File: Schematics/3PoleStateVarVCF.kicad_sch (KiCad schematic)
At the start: 127 parts, among them J54 Conn_01x04, J55 Conn_01x03, U270 DG212C, U277 DG212C, U32 SSI2164, U33 TL072, U34 TL074, U35 TL074, U36 TL074, U37 TL072, U38 TL074, U39 SSI2164, U42 TL072, U43 TL072

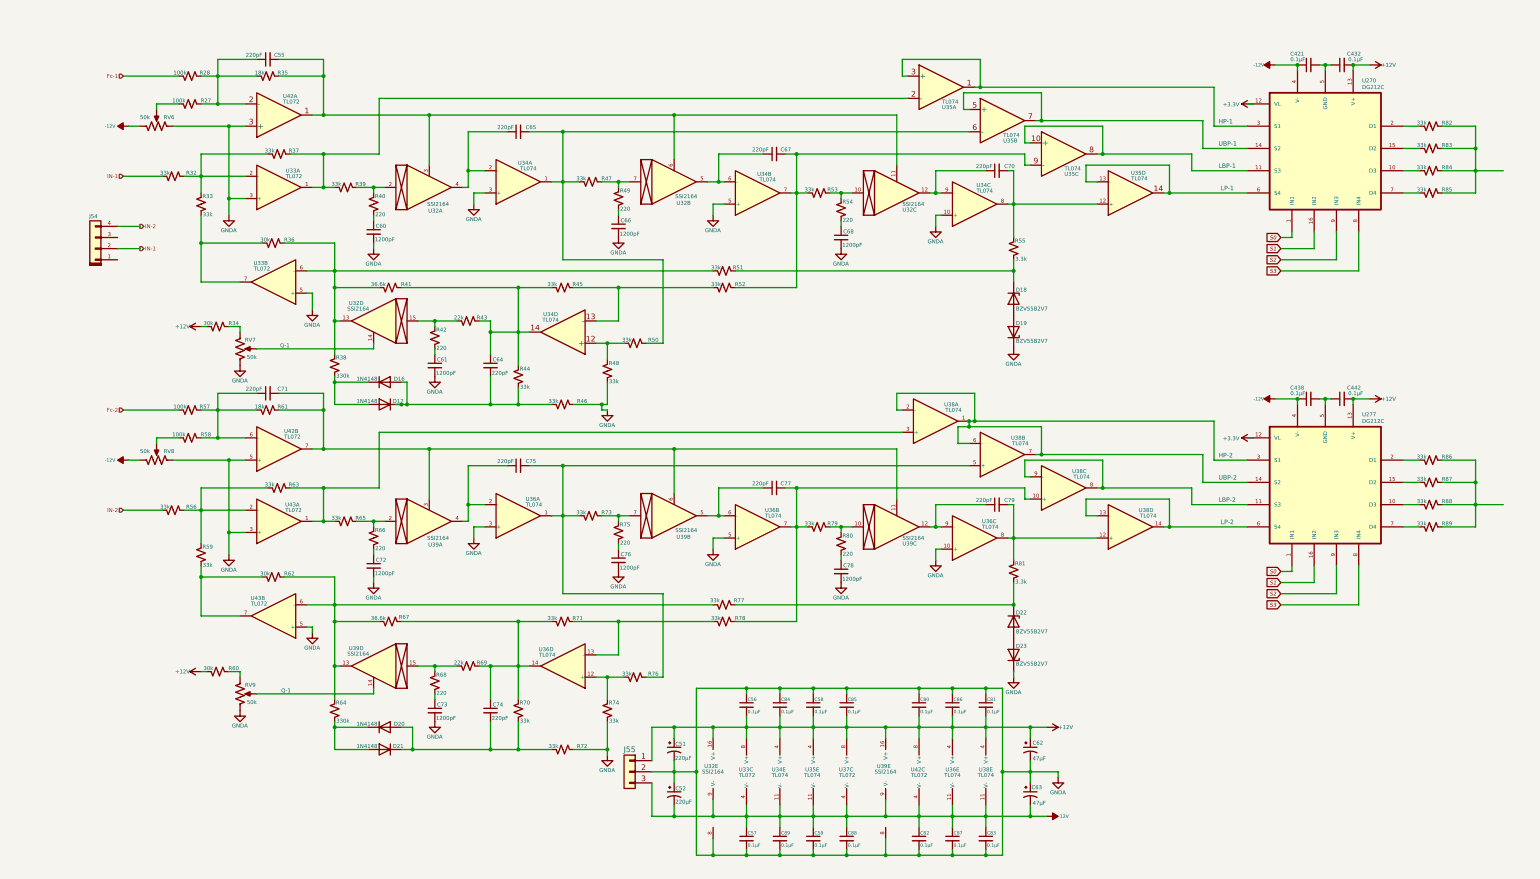
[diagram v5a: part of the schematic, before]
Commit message: Finalized first filter design.  Setep for filter testing.
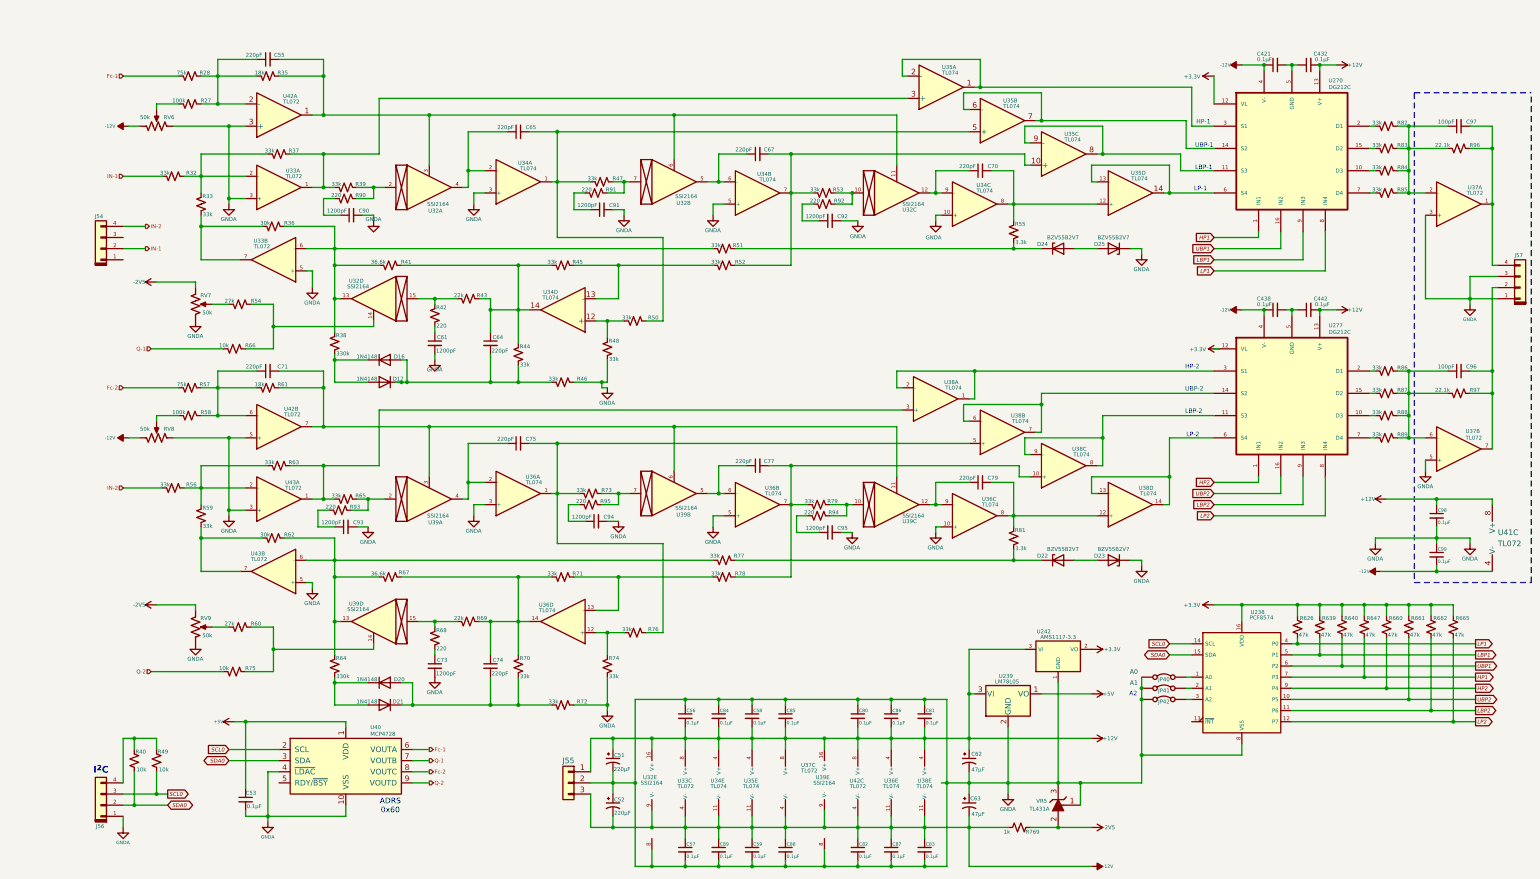
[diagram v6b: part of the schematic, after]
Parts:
- removed C60, C66, C68, C72, C76, C78: 1200pF, symbol Device:C_Small
- removed D18, D19: BZV55B2V7, Diode_SMD:D_MiniMELF, symbol Diode:BZV55B2V7
- removed R34: 30k, symbol Device:R_Small_US
- removed R80: 220, symbol Device:R_Small_US
- added C53, C98, C99: 0.1µF, symbol Device:C_Small
- added C90, C91, C92, C93, C94, C95: 1200pF, symbol Device:C_Small
- added C96, C97: 100pF, symbol Device:C_Small
- added D24, D25: BZV55B2V7, Diode_SMD:D_MiniMELF, symbol Diode:BZV55B2V7
- added J56: Conn_01x04, symbol Connector_keyed_kicad_sym:Conn_01x04
- added J57: Conn_01x04, symbol My Connectors:Conn_01x04
- added JP40, JP41, JP42: Jumper_2_Bridged, symbol Jumper:Jumper_2_Bridged
- added R626, R639, R640, R647, R660, R661, R662, R665: 47k, symbol Device:R_Small_US
- added R769: 1k, symbol Device:R_Small_US
- added R90, R91, R92, R93, R94, R95: 220, symbol Device:R_Small_US
- added R96, R97: 22.1k, symbol Device:R_Small_US
- added U238: PCF8574, symbol Interface_Expansion:PCF8574
- added U239: LM78L05, Package_TO_SOT_THT:TO-92_Inline, symbol Regulator_Linear:LM78L05_TO92
- added U242: AMS1117-3.3, Package_TO_SOT_SMD:SOT-223-3_TabPin2, symbol Regulator_Linear:AMS1117-3.3
- added unit 2 of U37
- added unit 1 of U37
- added U40: MCP4728, Package_SO:MSOP-10_3x3mm_P0.5mm, symbol MyDac:MCP4728
- added U41: TL072, symbol Amplifier_Operational:TL072
- added VR5: TL431A, digikey-footprints:TO-92-3_Formed_Leads, symbol dk_PMIC-Voltage-Reference:TL431CLPM
- R28, R57: value 100k -> 75k
- R40, R49, R66, R75: value 220 -> 10k
- R54: value 220 -> 27k
- R60: value 30k -> 27k
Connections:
- net +12V: now also C98.1, U239.3 (VI), U242.3 (VI), U41.8 (V+); no longer R60.2
- net +3.3V: now also R626.1, R639.1, R640.1, R647.1, R660.1, R661.1, R662.1, R665.1, U238.16 (VDD), U242.2 (VO)
- net -12V: now also C99.2, R769.1, U41.4 (V-)
- net Fc-1: now also U40.6 (VOUTA)
- net Fc-2: now also U40.8 (VOUTC)
- net GNDA: now also C53.2, C90.2, C91.2, C92.2, C93.2, C94.2, C95.2, C98.2, C99.1, D25.1 (K), J56.1 (Pin_1), J57.1 (Pin_1), J57.3 (Pin_3), JP40.1 (A), JP41.1 (A), JP42.1 (A), U238.8 (VSS), U239.2 (GND), U242.1 (GND), U37.3 (+), U37.5 (+), U40.10 (VSS), U40.4 (~{LDAC}), VR5.1 (REF), VR5.3 (K)
- net at R73.1, U39.7: now also R95.1; no longer R75.1
- net Q-2: now reaches R75.2
- net Q-2: now also U40.9 (VOUTD)
- net at R82.1, R83.1, R84.1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: now also C97.1, R96.2, U37.2 (-)
- net at R53.1, U32.10: now also R92.1; no longer R54.1
- net at R54.2: now also RV7. (2)
- net at R79.1, U39.10: now also R94.1
- net at U270.14 (S2), U35.7: now also U35.6 (-); no longer U35.5 (+)
- net at C65.2, R47.2, R50.1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: now also U35.5 (+); no longer U35.6 (-)
- net at R51.1, R55.2: now also D24.1 (K)
- net at U270.11 (S3), U35.8: now also U35.9 (-); no longer U35.10 (+)
- net at U270.3 (S1), U35.1: now also U35.2 (-); no longer U35.3 (+)
- net at R86.1, R87.1, R88.1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: now also C96.1, R97.2, U37.6 (-)
- net at R39.1, U32.2: now also R90.1; no longer R40.1
- net SDA0: now reaches R40.2
- net SDA0: now also J56.2 (Pin_2), U238.15 (SDA), U40.3 (SDA)
- net at U277.14 (S2), U38.6 (-), U38.7: no longer U277.3 (S1), U38.1, U38.2 (-)
- net at C67.2, R52.1, R53.2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: now also U35.10 (+); no longer U35.9 (-)
- net at R65.1, U39.2: now also R93.1; no longer R66.1
- net Q-1: now reaches R66.2
- net Q-1: now also U40.7 (VOUTB)
- net at U32.14: now also R54.1, R66.1; no longer RV7. (2)
- net at U39.14: now also R60.1, R75.1; no longer RV9. (2)
- net at R47.1, U32.7: now also R91.1; no longer R49.1
- net SCL0: now reaches R49.2
- net SCL0: now also J56.3 (Pin_3), U238.14 (SCL), U40.2 (SCL)
- net at R37.1, R39.2, U33.1: now also U35.3 (+); no longer U35.2 (-)
- net S0 renamed HP1
- net HP1: now also R647.2, U238.7 (P3); no longer U277.1 (IN1)
- net S1 renamed UBP1
- net UBP1: now also R640.2, U238.6 (P2); no longer U277.16 (IN2)
- net S2 renamed LBP1
- net LBP1: now also R639.2, U238.5 (P1); no longer U277.9 (IN3)
- net S3 renamed LP1
- net LP1: now also R626.2, U238.4 (P0); no longer U277.8 (IN4)
- new net: C96.2, J57.2 (Pin_2), R97.1, U37.7
- new net: C97.2, J57.4 (Pin_4), R96.1, U37.1
- new net: C91.1, R91.2
- new net: C93.1, R93.2
- new net: R60.2, RV9. (2)
- new net: D24.2 (A), D25.2 (A)
- new net: JP40.2 (B), U238.1 (A0)
- new net: C92.1, R92.2
- new net: C95.1, R94.2
- new net: JP41.2 (B), U238.2 (A1)
- new net: JP42.2 (B), U238.3 (A2)
- new net: U277.3 (S1), U38.1, U38.2 (-)
- new net: C94.1, R95.2
- new net: C90.1, R90.2
- new net: J56.4 (Pin_4), R40.1, R49.1
- new net +5V: C53.1, U239.1 (VO), U40.1 (VDD)
- new net -2V5: R769.2, RV7. (2), RV9. (2), VR5.2 (A)
- new net HP2: R660.2, U238.9 (P4), U277.1 (IN1)
- new net LBP2: R662.2, U238.11 (P6), U277.9 (IN3)
- new net LP2: R665.2, U238.12 (P7), U277.8 (IN4)
- new net UBP2: R661.2, U238.10 (P5), U277.16 (IN2)
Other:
- note added: "A0"
- note added: "A1"
- note added: "A2"
- note added: "ADRS 0x60"
- note added: "I^{2}C"
- note removed: "Q-1"
- moved on the sheet: C421, C432, C438, C442, C51, C52, C56, C57, C58, C59, C61, C62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

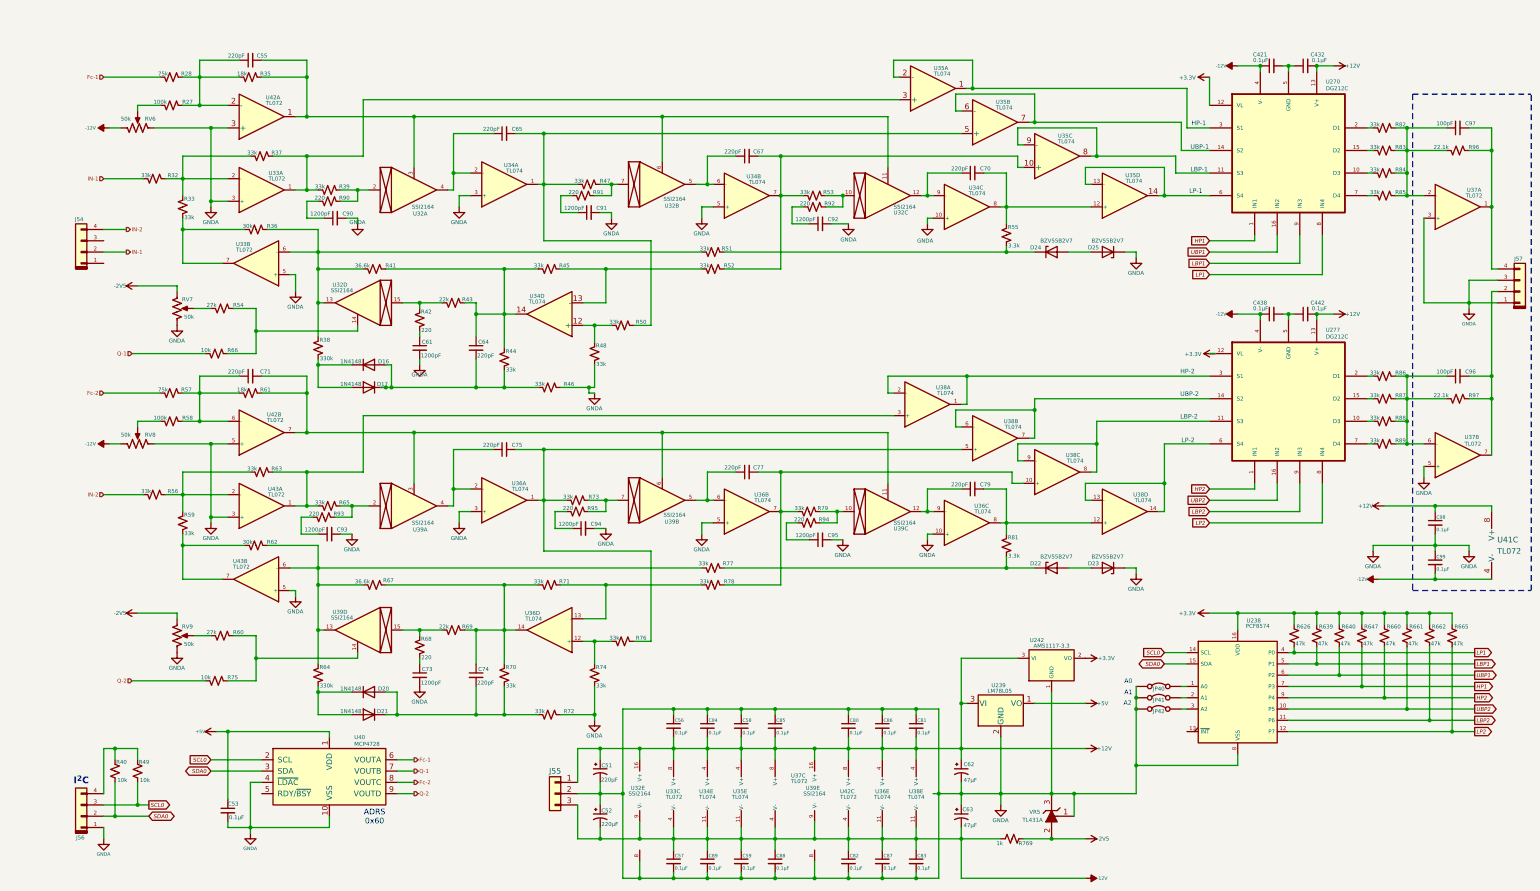
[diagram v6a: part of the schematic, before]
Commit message: Fixed schematic errors.
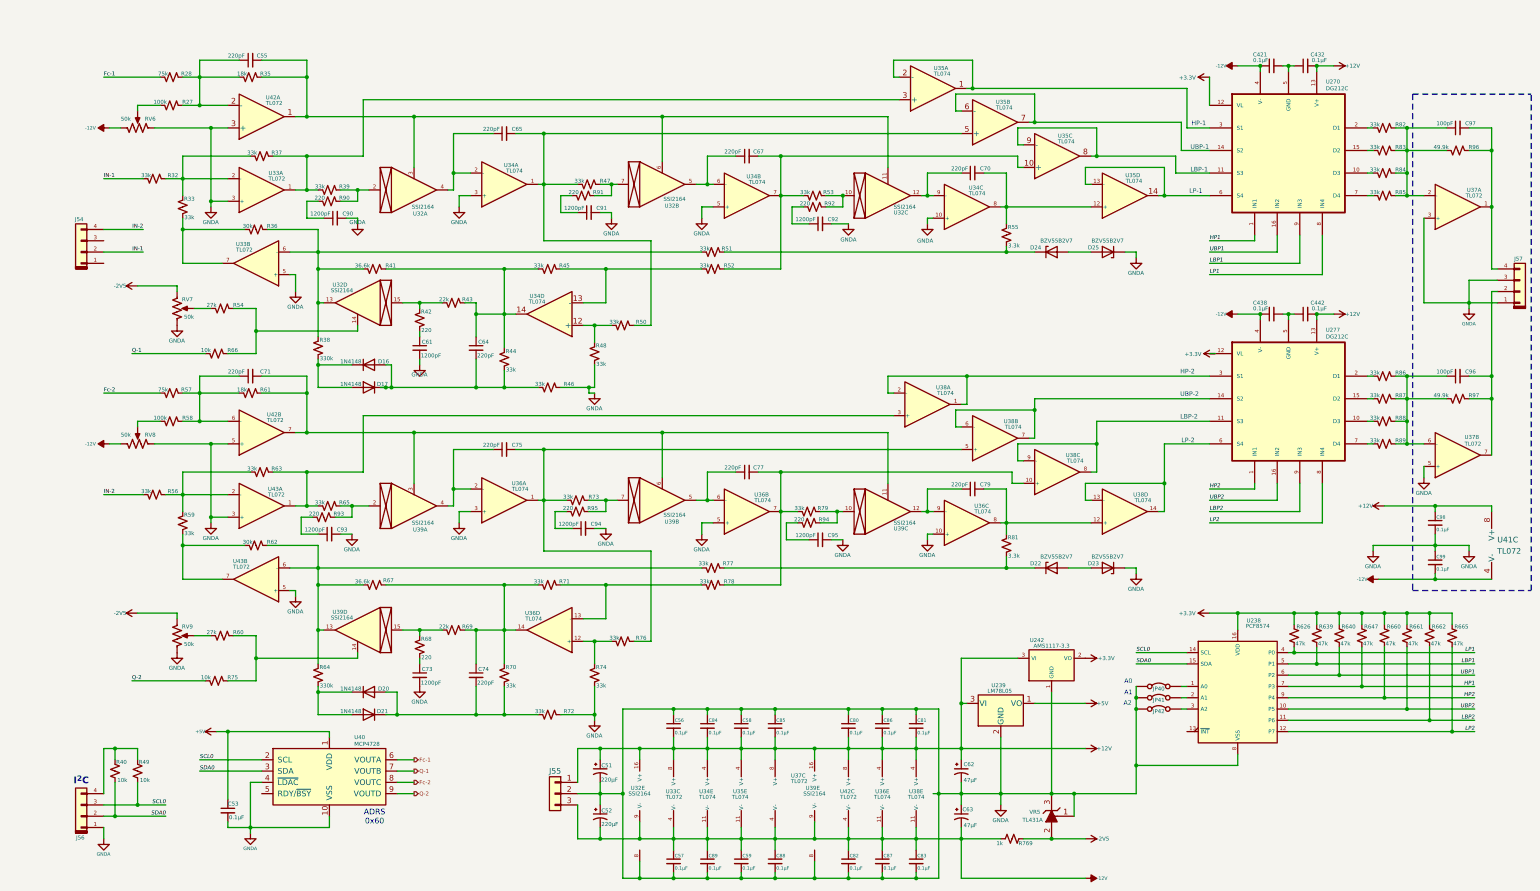
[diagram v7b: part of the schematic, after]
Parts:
- R96, R97: value 22.1k -> 49.9k

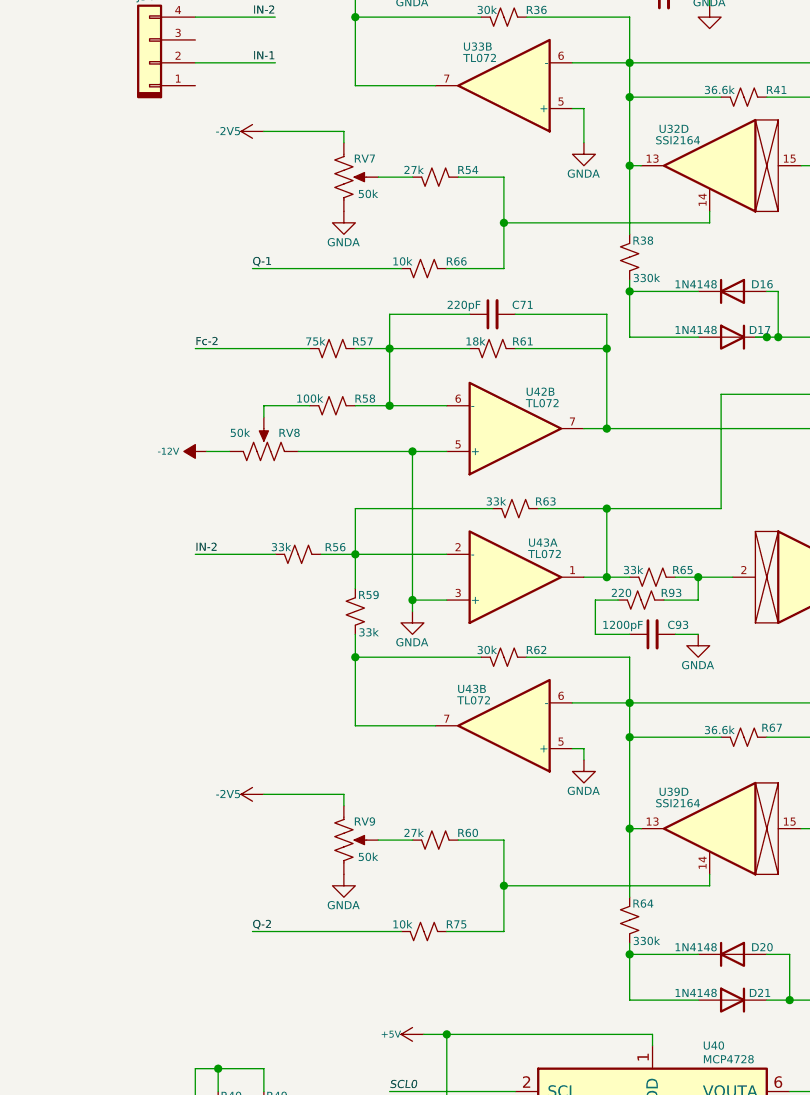
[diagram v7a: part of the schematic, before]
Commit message: Refactored hardware and software.  Improved Launch Control XL configuration and control.
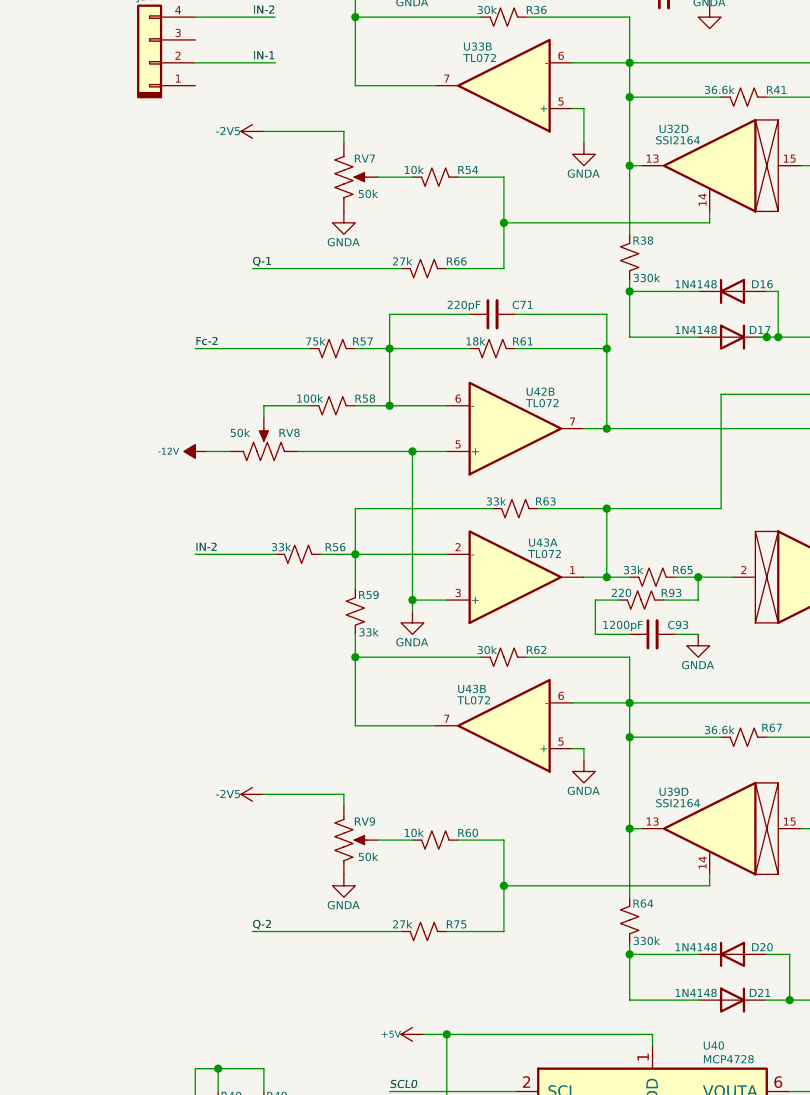
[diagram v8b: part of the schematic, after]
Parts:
- R54, R60: value 27k -> 10k
- R66, R75: value 10k -> 27k
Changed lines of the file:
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@@
 			)
 		)
-		(property "Value" "27k"
+		(property "Value" "10k"
 			(at 46.99 71.628 90)
 			(effects
@@
 			)
 		)
-		(property "Value" "10k"
+		(property "Value" "27k"
 			(at 45.72 155.448 90)
 			(effects
@@
 			)
 		)
-		(property "Value" "10k"
+		(property "Value" "27k"
 			(at 45.72 81.788 90)
 			(effects
@@
 			)
 		)
-		(property "Value" "27k"
+		(property "Value" "10k"
 			(at 46.99 145.288 90)
 			(effects
